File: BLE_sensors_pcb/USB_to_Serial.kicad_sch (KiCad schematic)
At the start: 3 parts, among them U7 MCP2221AxST

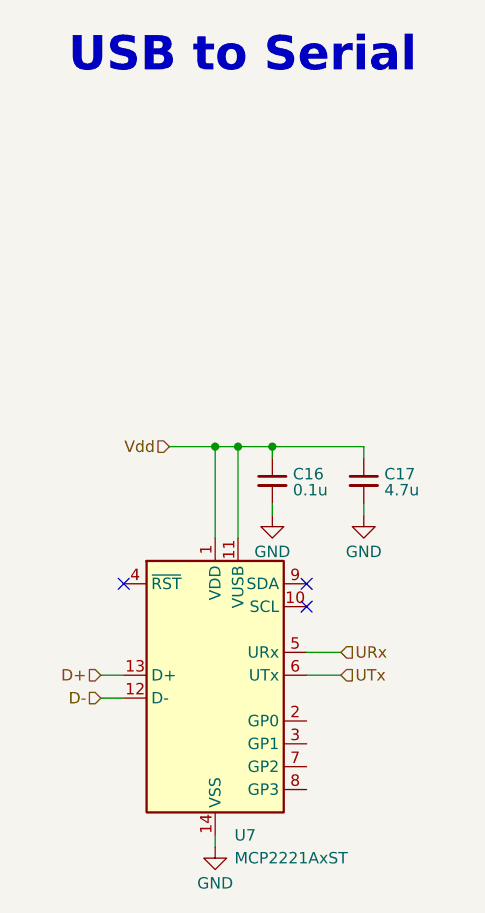
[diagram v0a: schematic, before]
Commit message: Footprints and some pcb placement
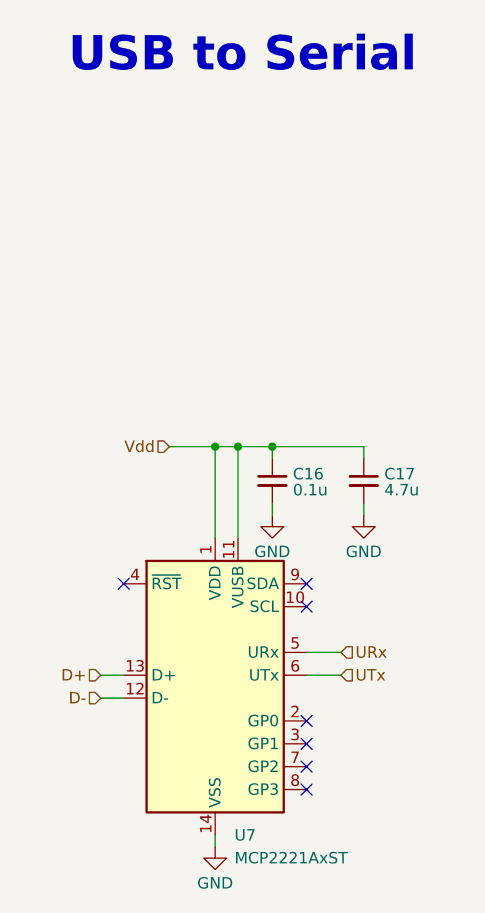
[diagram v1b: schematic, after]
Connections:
- no-connect marks 3 -> 7
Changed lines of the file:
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@@
+	)
+	(no_connect
+		(at 152.4 116.84)
+	)
+	(no_connect
+		(at 152.4 109.22)
 	)
 	(no_connect
@@
 	)
 	(no_connect
+		(at 152.4 114.3)
+	)
+	(no_connect
 		(at 152.4 96.52)
 	)
 	(no_connect
+		(at 152.4 111.76)
+	)
+	(no_connect

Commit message: Initial pcb placement
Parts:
- added R15, R16: 100R, Resistor_SMD:R_0603_1608Metric, symbol Device:R_Small
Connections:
- net URx: now also R15.2; no longer U7.5 (URx)
- net UTx: now also R16.2; no longer U7.6 (UTx)
- new net: R15.1, U7.5 (URx)
- new net: R16.1, U7.6 (UTx)
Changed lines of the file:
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@@
 	(wire
 		(pts
-			(xy 152.4 104.14) (xy 156.21 104.14)
+			(xy 152.4 104.14) (xy 154.94 104.14)
 		)
 		(stroke
@@
 	(wire
 		(pts
+			(xy 160.02 104.14) (xy 163.83 104.14)
+		)
+		(stroke
+			(width 0)
+			(type default)
+		)
+	)
+	(wire
+		(pts
 			(xy 158.75 80.01) (xy 158.75 78.74)
 		)
@@
 	(wire
 		(pts
-			(xy 152.4 101.6) (xy 156.21 101.6)
+			(xy 152.4 101.6) (xy 154.94 101.6)
 		)
 		(stroke
@@
 		(pts
 			(xy 158.75 78.74) (xy 148.59 78.74)
+		)
+		(stroke
+			(width 0)
+			(type default)
+		)
+	)
+	(wire
+		(pts
+			(xy 160.02 101.6) (xy 163.83 101.6)
 		)
 		(stroke
@@
 	(hierarchical_label "UTx"
 		(shape input)
-		(at 156.21 104.14 0)
+		(at 163.83 104.14 0)
 		(effects
 			(font
@@
 	(hierarchical_label "URx"
 		(shape input)
-		(at 156.21 101.6 0)
+		(at 163.83 101.6 0)
 		(effects
 			(font
@@
 	)
 	(symbol
+		(lib_id "Device:R_Small")
+		(at 157.48 104.14 90)
+		(unit 1)
+		(exclude_from_sim no)
+		(in_bom yes)
+		(on_board yes)
+		(dnp no)
+		(property "Reference" "R16"
+			(at 157.48 106.426 90)
+			(effects
+				(font
+					(size 1.27 1.27)
+				)
+			)
+		)
+		(property "Value" "100R"
+			(at 157.48 108.966 90)
+			(effects
+				(font
+					(size 1.27 1.27)
+				)
+			)
+		)
+		(property "Footprint" "Resistor_SMD:R_0603_1608Metric"
+			(at 157.48 104.14 0)
+			(effects
+				(font
+					(size 1.27 1.27)
+				)
+				(hide yes)
+			)
+		)
+		(property "Datasheet" "~"
+			(at 157.48 104.14 0)
+			(effects
+				(font
+					(size 1.27 1.27)
+				)
+				(hide yes)
+			)
+		)
+		(property "Description" "Resistor, small symbol"
+			(at 157.48 104.14 0)
+			(effects
+				(font
+					(size 1.27 1.27)
+				)
+				(hide yes)
+			)
+		)
+		(pin "2"
+		)
+		(pin "1"
+		)
+		(instances
+			(project "BLE_sensors"
+				(path "/06b47d3c-6b7b-411b-8755-cae193722202/4f72fd42-d729-49de-850d-d28e88b85ae2"
+					(reference "R16")
+					(unit 1)
+				)
+			)
+		)
+	)
+	(symbol
 		(lib_id "power:GND")
 		(at 158.75 86.36 0)
@@
 					(unit 1)
 				)
+			)
+		)
+	)
+	(symbol
+		(lib_id "Device:R_Small")
+		(at 157.48 101.6 90)
+		(unit 1)
+		(exclude_from_sim no)
+		(in_bom yes)
+		(on_board yes)
+		(dnp no)
+		(property "Reference" "R15"
+			(at 157.48 99.822 90)
+			(effects
+				(font
+					(size 1.27 1.27)
+				)
+			)
+		)
+		(property "Value" "100R"
+			(at 157.48 97.79 90)
+			(effects
+				(font
+					(size 1.27 1.27)
+				)
+			)
+		)
+		(property "Footprint" "Resistor_SMD:R_0603_1608Metric"
+			(at 157.48 101.6 0)
+			(effects
+				(font
+					(size 1.27 1.27)
+				)
+				(hide yes)
+			)
+		)
+		(property "Datasheet" "~"
+			(at 157.48 101.6 0)
+			(effects
+				(font
+					(size 1.27 1.27)
+				)
+				(hide yes)
+			)
+		)
+		(property "Description" "Resistor, small symbol"
+			(at 157.48 101.6 0)
+			(effects
+				(font
+					(size 1.27 1.27)
+				)
+				(hide yes)
+			)
+		)
+		(pin "2"
+		)
+		(pin "1"
+		)
+		(instances
+			(project "BLE_sensors"
+				(path "/06b47d3c-6b7b-411b-8755-cae193722202/4f72fd42-d729-49de-850d-d28e88b85ae2"
+					(reference "R15")
+					(unit 1)
+				)
